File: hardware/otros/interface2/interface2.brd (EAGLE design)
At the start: 73.6 x 18.7 mm, 6 parts

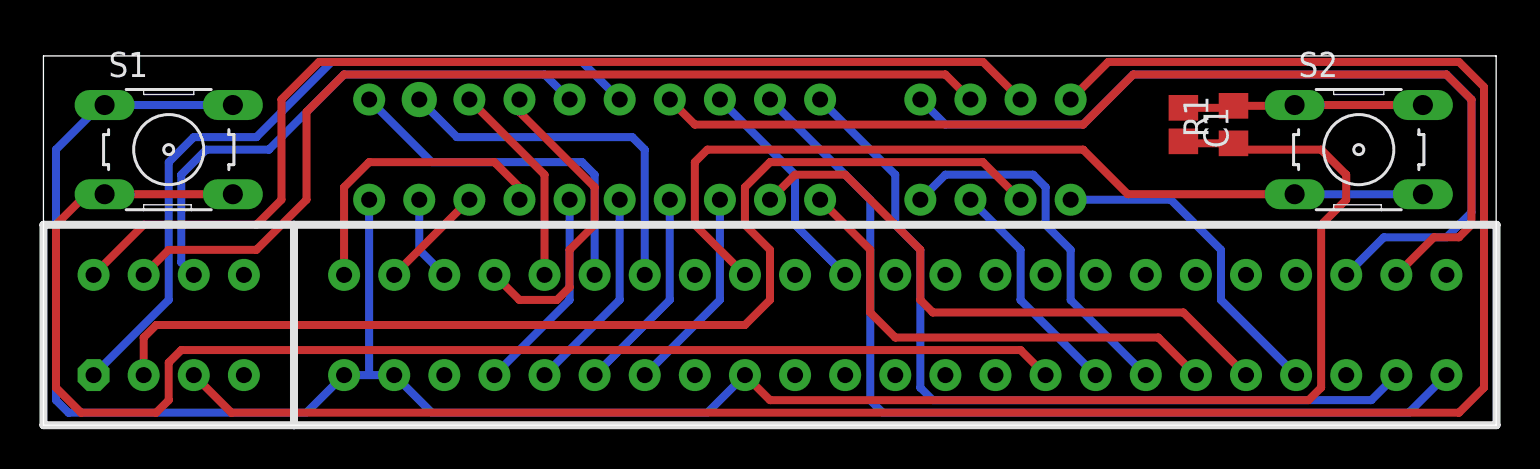
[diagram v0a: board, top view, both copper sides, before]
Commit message: 
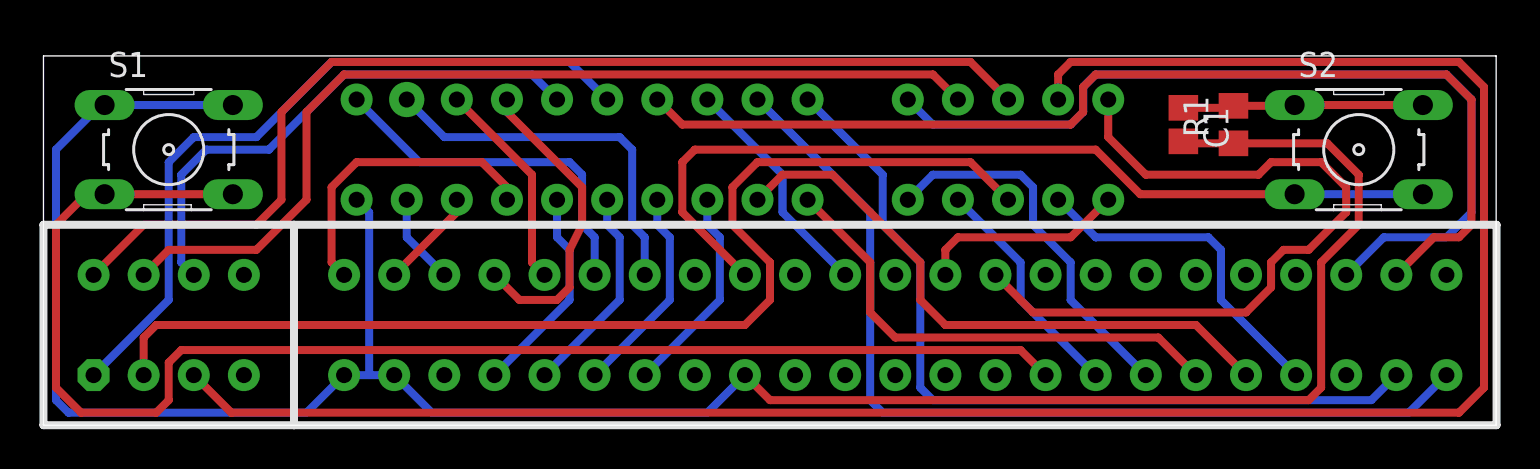
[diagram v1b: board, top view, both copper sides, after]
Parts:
- moved U$1 0.63 mm to (33.7, 14.0)
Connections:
- new net RD: U$1.RD, U$3.B18
- new net WR: U$1.WR, U$3.B19
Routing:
- net WR: track 0.00 -> 38.2 mm
- net RD: track 0.00 -> 10.6 mm
- net A8: track 43.4 -> 44.8 mm
- net A10: track 54.0 -> 55.3 mm
- net VCC: track 104.2 -> 105.6 mm
- net GND: track 119.3 -> 120.5 mm
- net A15: track 55.2 -> 54.2 mm
- net NMI: track 44.9 -> 45.8 mm
- net A13: track 49.2 -> 48.6 mm
- net ROMCS: track 16.6 -> 17.2 mm
- net D7: track 27.7 -> 27.0 mm
- net A14: track 38.1 -> 37.5 mm

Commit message: 
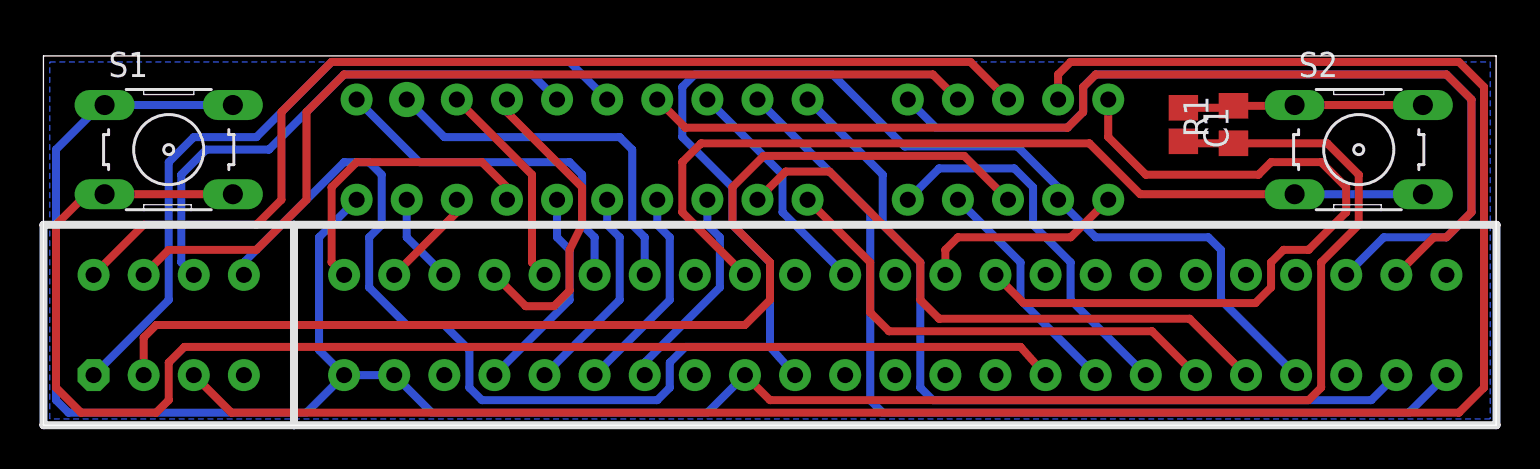
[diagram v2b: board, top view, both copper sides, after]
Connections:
- net ROMCS: now also U$3.A15, U$3.B4
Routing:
- net ROMCS: track 17.2 -> 98.1 mm
- net GND: track 120.5 -> 121.5 mm
- added copper zone on layer 16, net GND

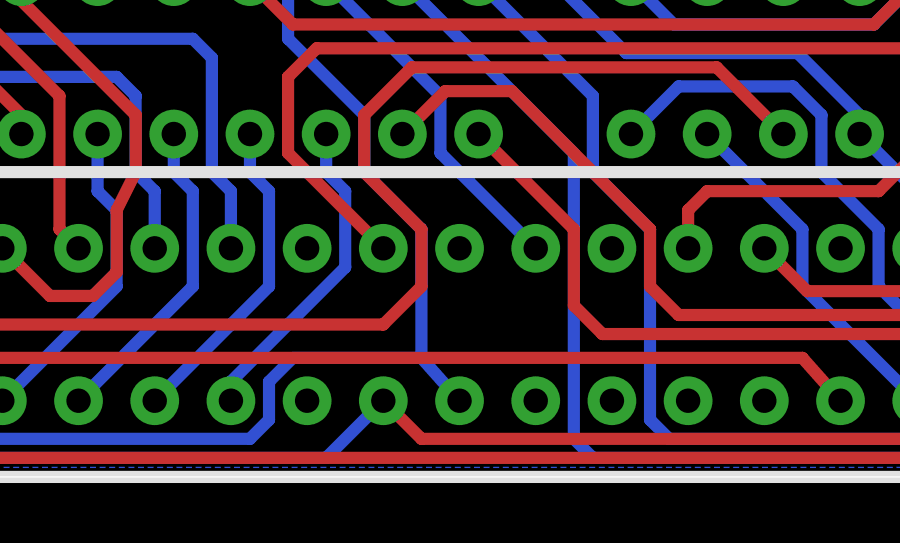
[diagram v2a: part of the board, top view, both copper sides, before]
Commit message: 
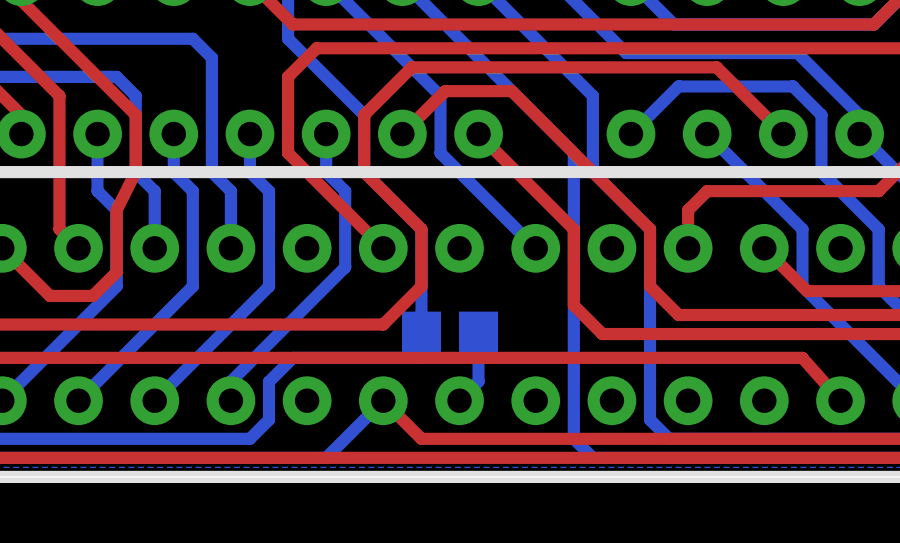
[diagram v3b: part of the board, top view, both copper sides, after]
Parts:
- added R2: (no value), rcl:R0805
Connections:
- new net N$1: R2.2, U$3.A15
- net ROMCS: now also R2.1; no longer U$3.A15
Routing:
- net N$1: track 0.00 -> 2.48 mm
- net ROMCS: track 98.1 -> 96.2 mm
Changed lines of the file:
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@@
 <element name="R1" library="rcl" package="R0805" value="1K" x="60.325" y="15.24" rot="R90"/>
 <element name="C1" library="resistor" package="C0805" value="4.7nF" x="57.785" y="15.24" rot="R270"/>
+<element name="R2" library="rcl" package="R0805" value="" x="37.7825" y="4.7625" rot="MR180"/>
 </elements>
 <signals>
@@
 <wire x1="59.055" y1="9.525" x2="53.34" y2="9.525" width="0.4064" layer="16"/>
 <wire x1="53.34" y1="9.525" x2="51.435" y2="11.43" width="0.4064" layer="16"/>
-<contactref element="U$3" pad="A15"/>
 <contactref element="U$3" pad="B4"/>
 <wire x1="51.435" y1="11.43" x2="51.435" y2="12.065" width="0.4064" layer="16"/>
@@
 <wire x1="34.925" y1="12.065" x2="34.925" y2="10.16" width="0.4064" layer="16"/>
 <wire x1="34.925" y1="10.16" x2="36.83" y2="8.255" width="0.4064" layer="16"/>
-<wire x1="36.83" y1="8.255" x2="36.83" y2="3.96875" width="0.4064" layer="16"/>
-<wire x1="36.83" y1="3.96875" x2="38.1" y2="2.54" width="0.4064" layer="16"/>
 <wire x1="10.16" y1="7.62" x2="10.16" y2="8.255" width="0.4064" layer="16"/>
 <wire x1="10.16" y1="8.255" x2="15.24" y2="13.335" width="0.4064" layer="16"/>
@@
 <wire x1="31.75" y1="3.175" x2="32.54375" y2="3.96875" width="0.4064" layer="16"/>
 <wire x1="36.83" y1="3.96875" x2="32.54375" y2="3.96875" width="0.4064" layer="16"/>
+<contactref element="R2" pad="1"/>
+<wire x1="36.83" y1="8.255" x2="36.83" y2="4.765" width="0.4064" layer="16"/>
+<wire x1="36.83" y1="4.765" x2="36.8325" y2="4.7625" width="0.4064" layer="16"/>
+<wire x1="36.83" y1="4.765" x2="36.83" y2="3.96875" width="0.4064" layer="16"/>
 </signal>
 <signal name="RD">
@@
 <wire x1="53.975" y1="14.605" x2="53.975" y2="16.51" width="0.4064" layer="1"/>
 </signal>
+<signal name="N$1">
+<contactref element="U$3" pad="A15"/>
+<contactref element="R2" pad="2"/>
+<wire x1="38.7325" y1="4.7625" x2="38.7325" y2="3.1725" width="0.4064" layer="16"/>
+<wire x1="38.7325" y1="3.1725" x2="38.1" y2="2.54" width="0.4064" layer="16"/>
+</signal>
 </signals>

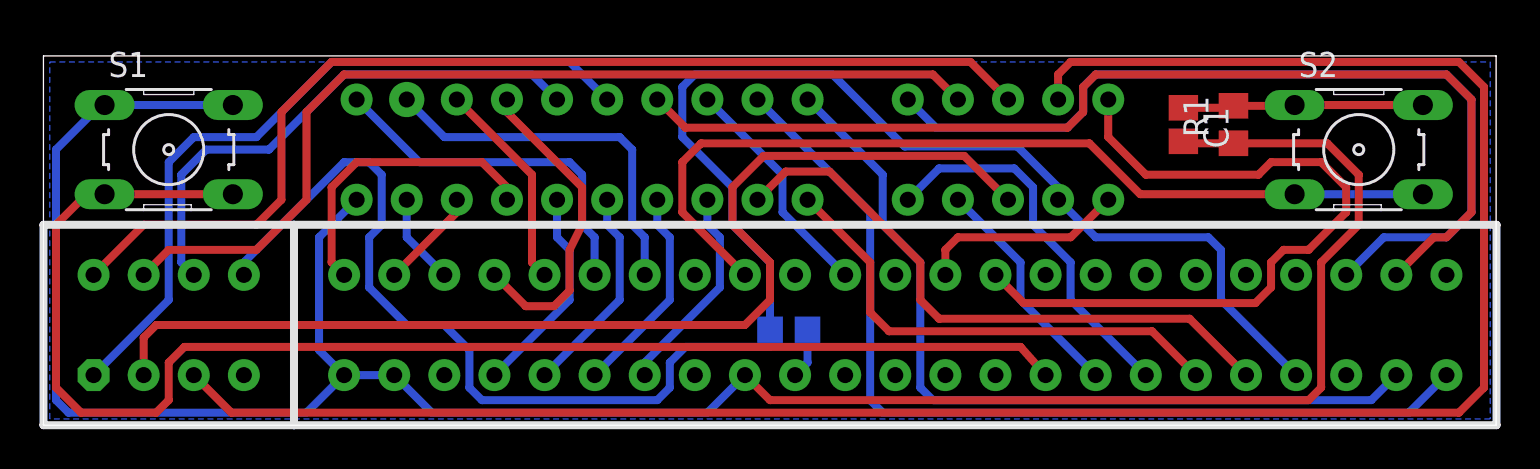
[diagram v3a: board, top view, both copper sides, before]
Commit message: 
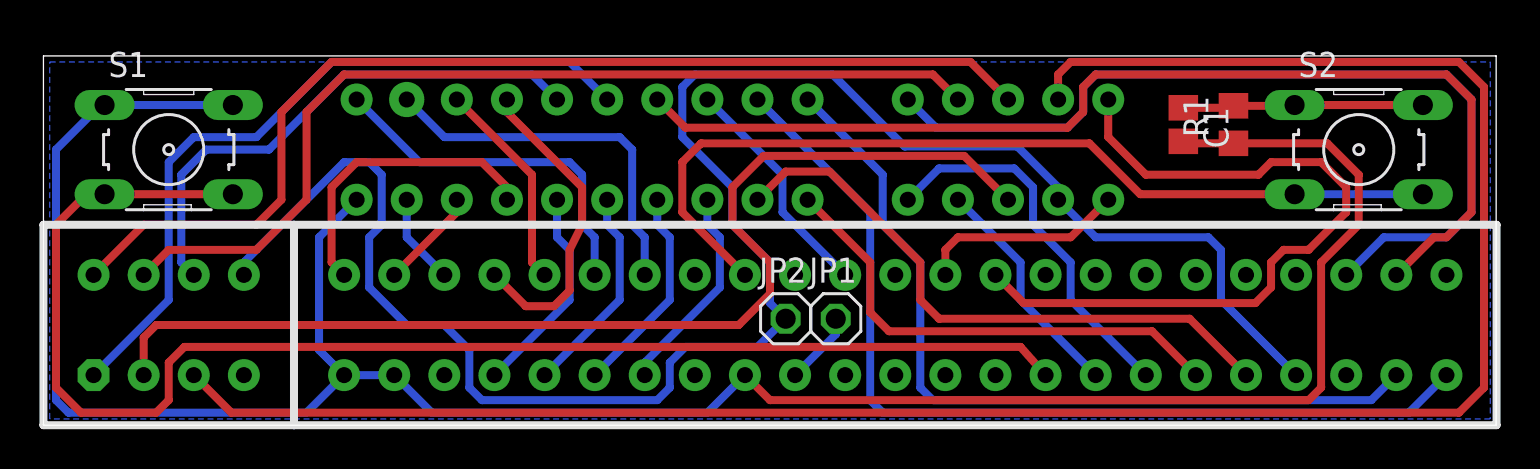
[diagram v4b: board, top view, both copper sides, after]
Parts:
- removed R2: (no value), rcl:R0805
- added JP1, JP2: (no value), pinhead:1X01
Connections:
- net N$1: now also JP1.1; no longer R2.2
- net ROMCS: now also JP2.1; no longer R2.1
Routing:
- net N$1: track 2.48 -> 3.71 mm
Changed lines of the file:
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@@
 <element name="R1" library="rcl" package="R0805" value="1K" x="60.325" y="15.24" rot="R90"/>
 <element name="C1" library="resistor" package="C0805" value="4.7nF" x="57.785" y="15.24" rot="R270"/>
-<element name="R2" library="rcl" package="R0805" value="" x="37.7825" y="4.7625" rot="MR180"/>
+<element name="JP2" library="pinhead" package="1X01" value="" x="37.62375" y="5.3975"/>
+<element name="JP1" library="pinhead" package="1X01" value="" x="40.16375" y="5.3975"/>
 </elements>
 <signals>
@@
 <wire x1="36.5125" y1="13.6525" x2="46.6725" y2="13.6525" width="0.4064" layer="1"/>
 <wire x1="46.6725" y1="13.6525" x2="48.895" y2="11.43" width="0.4064" layer="1"/>
-<wire x1="36.83" y1="6.35" x2="35.56" y2="5.08" width="0.4064" layer="1"/>
-<wire x1="35.56" y1="5.08" x2="5.715" y2="5.08" width="0.4064" layer="1"/>
+<wire x1="36.83" y1="6.6675" x2="35.2425" y2="5.08" width="0.4064" layer="1"/>
+<wire x1="35.2425" y1="5.08" x2="5.715" y2="5.08" width="0.4064" layer="1"/>
 <wire x1="5.715" y1="5.08" x2="5.08" y2="4.445" width="0.4064" layer="1"/>
 <wire x1="5.08" y1="4.445" x2="5.08" y2="2.54" width="0.4064" layer="1"/>
-<wire x1="36.83" y1="6.35" x2="36.83" y2="8.255" width="0.4064" layer="1"/>
+<wire x1="36.83" y1="6.6675" x2="36.83" y2="8.255" width="0.4064" layer="1"/>
 <wire x1="36.83" y1="8.255" x2="34.925" y2="10.16" width="0.4064" layer="1"/>
 </signal>
@@
 <wire x1="31.75" y1="1.905" x2="31.75" y2="3.175" width="0.4064" layer="16"/>
 <wire x1="31.75" y1="3.175" x2="32.54375" y2="3.96875" width="0.4064" layer="16"/>
-<wire x1="36.83" y1="3.96875" x2="32.54375" y2="3.96875" width="0.4064" layer="16"/>
-<contactref element="R2" pad="1"/>
-<wire x1="36.83" y1="8.255" x2="36.83" y2="4.765" width="0.4064" layer="16"/>
-<wire x1="36.83" y1="4.765" x2="36.8325" y2="4.7625" width="0.4064" layer="16"/>
-<wire x1="36.83" y1="4.765" x2="36.83" y2="3.96875" width="0.4064" layer="16"/>
+<contactref element="JP2" pad="1"/>
+<wire x1="32.54375" y1="3.96875" x2="36.195" y2="3.96875" width="0.4064" layer="16"/>
+<wire x1="36.195" y1="3.96875" x2="37.62375" y2="5.3975" width="0.4064" layer="16"/>
+<wire x1="36.83" y1="8.255" x2="36.83" y2="6.19125" width="0.4064" layer="16"/>
+<wire x1="36.83" y1="6.19125" x2="37.62375" y2="5.3975" width="0.4064" layer="16"/>
 </signal>
 <signal name="RD">
@@
 <signal name="N$1">
 <contactref element="U$3" pad="A15"/>
-<contactref element="R2" pad="2"/>
-<wire x1="38.7325" y1="4.7625" x2="38.7325" y2="3.1725" width="0.4064" layer="16"/>
-<wire x1="38.7325" y1="3.1725" x2="38.1" y2="2.54" width="0.4064" layer="16"/>
+<contactref element="JP1" pad="1"/>
+<wire x1="40.16375" y1="5.3975" x2="40.16375" y2="4.60375" width="0.4064" layer="16"/>
+<wire x1="40.16375" y1="4.60375" x2="38.1" y2="2.54" width="0.4064" layer="16"/>
 </signal>
 </signals>

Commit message: 
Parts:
- C1: value 4.7nF -> 4.7uF
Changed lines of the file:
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@@
 <element name="U$1" library="8Bit_Parts" package="ZX_CARTRIDGE" value="ZX_CARTRIDGE" x="33.655" y="13.97" rot="MR180"/>
 <element name="R1" library="rcl" package="R0805" value="1K" x="60.325" y="15.24" rot="R90"/>
-<element name="C1" library="resistor" package="C0805" value="4.7nF" x="57.785" y="15.24" rot="R270"/>
+<element name="C1" library="resistor" package="C0805" value="4.7uF" x="57.785" y="15.24" rot="R270"/>
 <element name="JP2" library="pinhead" package="1X01" value="" x="37.62375" y="5.3975"/>
 <element name="JP1" library="pinhead" package="1X01" value="" x="40.16375" y="5.3975"/>

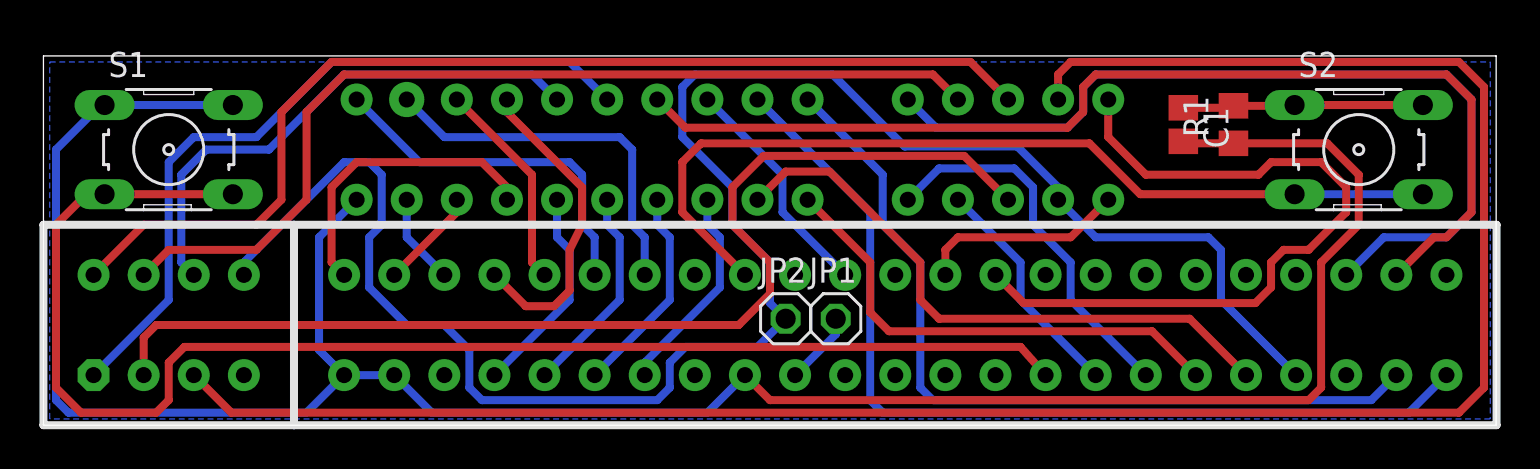
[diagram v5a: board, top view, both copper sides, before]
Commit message: 
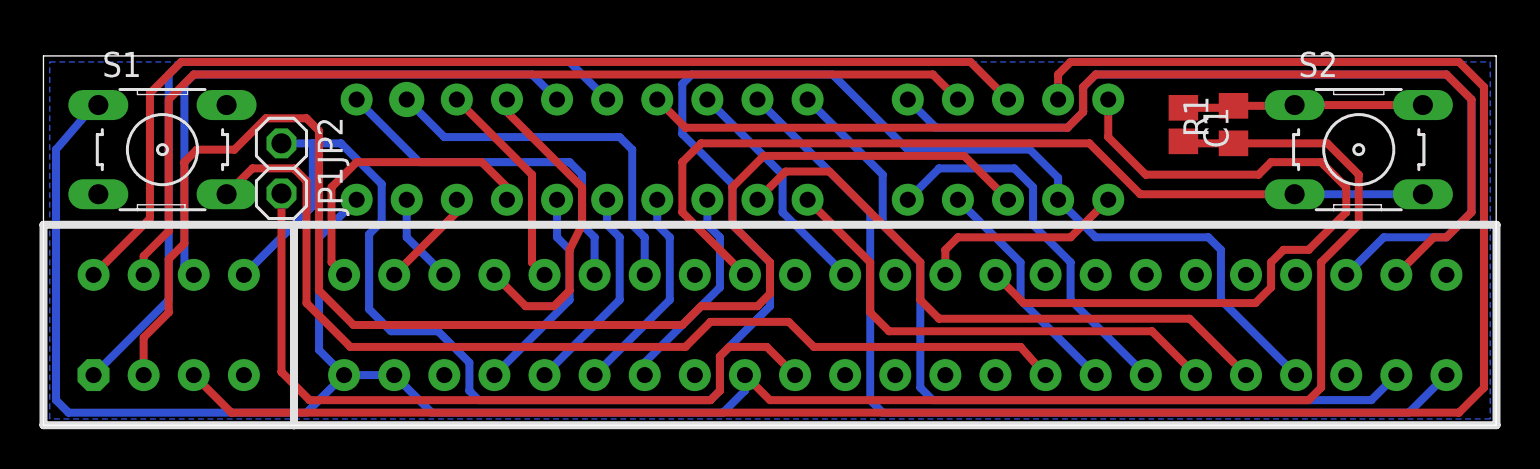
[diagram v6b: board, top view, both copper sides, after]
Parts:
- moved JP1 28.8 mm to (12.1, 11.7), turned to 270 degrees
- moved JP2 27.1 mm to (12.1, 14.3), turned to 270 degrees
- moved S1 0.32 mm to (6.03, 14.0)
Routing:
- net N$1: track 3.71 -> 38.4 mm
- net RESET: track 71.7 -> 51.1 mm
- net A12: track 56.3 -> 73.7 mm
- net GND: track 121.5 -> 115.3 mm
- net ROMCS: track 96.5 -> 99.6 mm
- net A14: track 37.5 -> 40.1 mm
- net D7: track 27.0 -> 29.5 mm
- net A13: track 48.6 -> 50.5 mm
- net A15: track 54.2 -> 55.3 mm

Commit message: 
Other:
- board text added: "AntonioVillena"
- board text added: "Interface II jul2015"
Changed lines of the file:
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@@
 <wire x1="73.64" y1="18.72" x2="0" y2="18.72" width="0" layer="20"/>
 <wire x1="0" y1="18.72" x2="0" y2="0" width="0" layer="20"/>
+<text x="71.755" y="4.28625" size="1.778" layer="22" rot="MR0">Interface II jul2015</text>
+<text x="44.45" y="4.28625" size="1.778" layer="22" rot="MR0">AntonioVillena</text>
 </plain>
 <attributes>
